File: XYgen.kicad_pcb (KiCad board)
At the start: 4 copper layers, 100 x 100 mm, 129 parts, among them J1 V_analog_in, J10 Mounting Hole, J11 Mounting Hole, J12 Mounting Hole, J13 Mounting Hole, J2 Ones, J3 Tens, J4 Hundreds, J5 Thousands, J6 Vin, J7 Blanking, J8 XOut, J9 YOut, Q1 MMBT3906, Q10 MMBT3906, Q11 MMBT3904, Q12 MMBT3906, Q13 MMBT3904, Q14 MMBFJ309, Q15 MMBT3904, Q2 MMBT3904, Q3 MMBT3906, Q4 MMBT3904, Q5 MMBT3906, Q6 MMBT3904, Q7 MMBFJ309, Q8 MMBT3906, Q9 MMBT3904, U1 40106, U10 LM358, U11 NE5532, U12 NE5532, U13 4052, U14 4052, U2 74HC123, U3 74HC08, U4 74HC32, U5 4040, U6 4511, U7 4051, U8 LM358, U9 LM358, Y1 32.768kHz

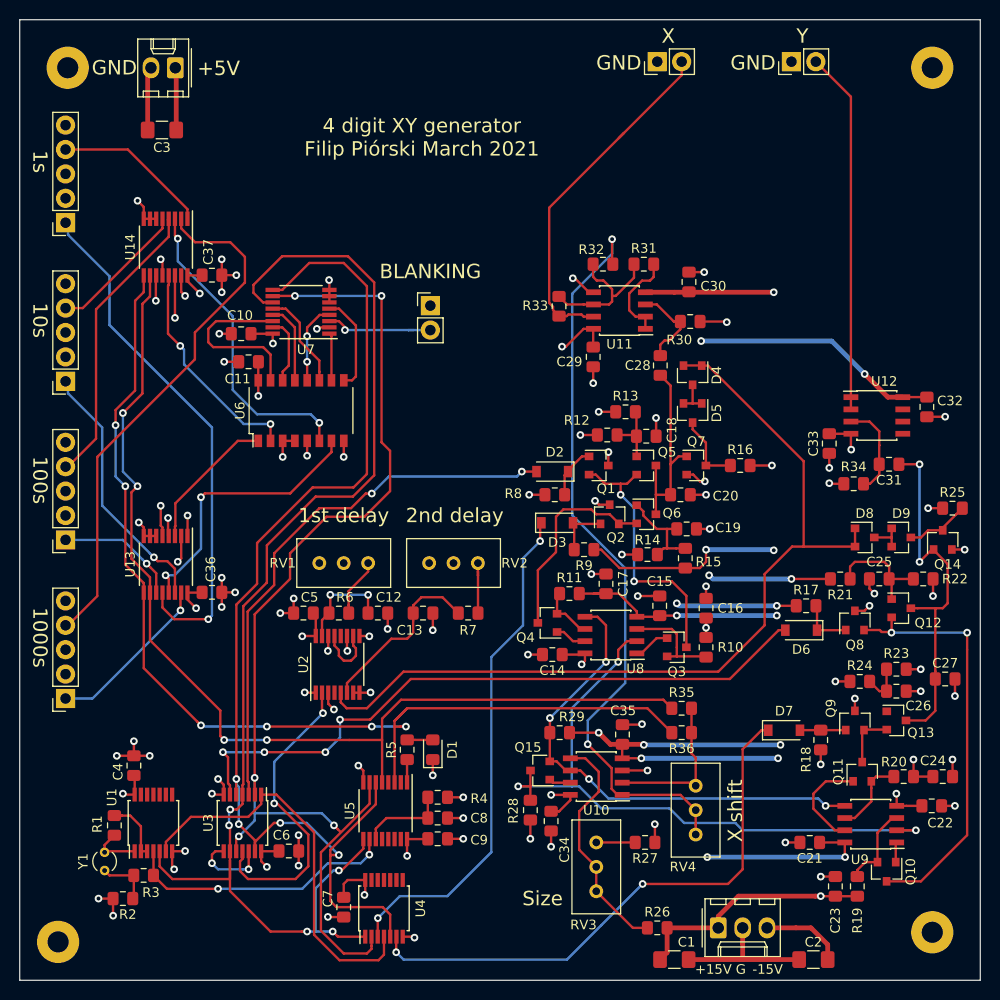
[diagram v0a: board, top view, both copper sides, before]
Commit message: Fixed some bugs, finished block symbols
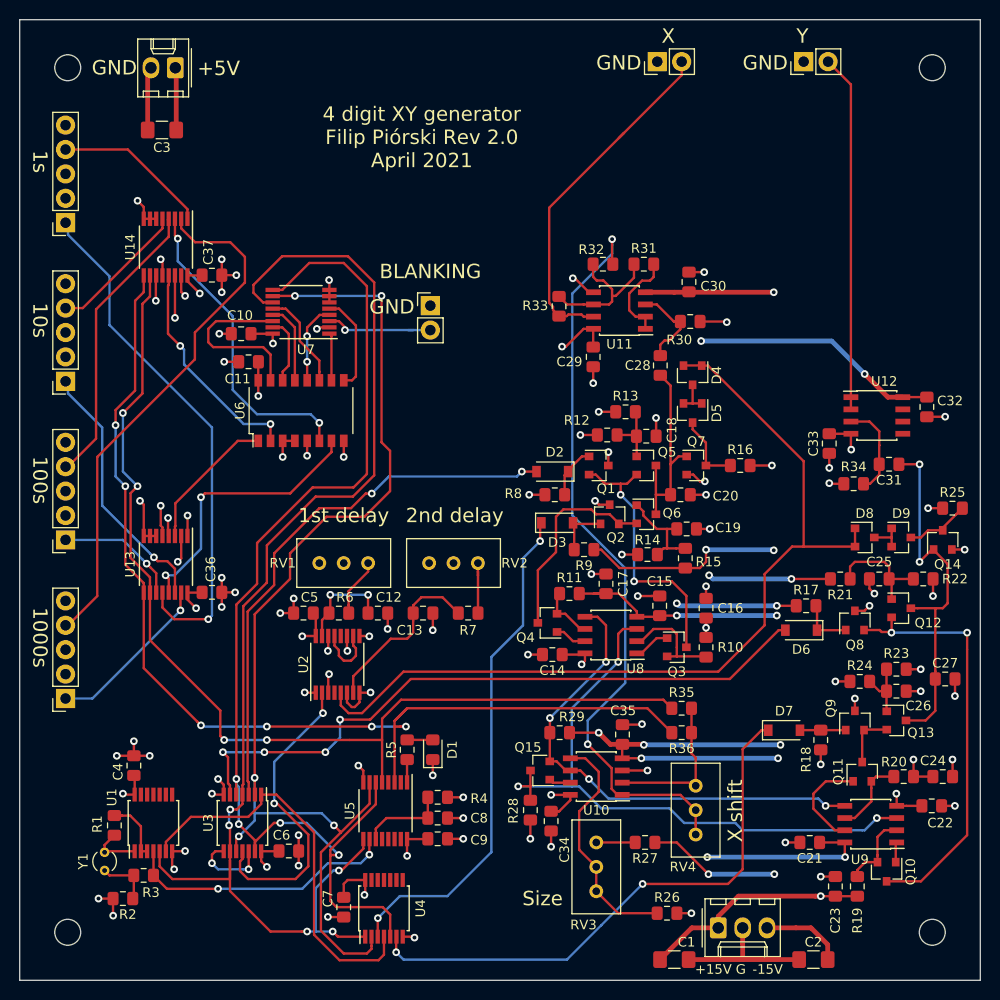
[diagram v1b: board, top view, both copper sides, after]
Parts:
- removed J10, J11, J12, J13: Mounting Hole, MountingHole:MountingHole_2.2mm_M2_Pad
- added H1: MountingHole, MountingHole:MountingHole_2.7mm_M2.5, F.Cu at (105.0, 40.0)
- added H2: MountingHole, MountingHole:MountingHole_2.7mm_M2.5, F.Cu at (105.0, 130.0)
- added H3: MountingHole, MountingHole:MountingHole_2.7mm_M2.5, F.Cu at (195.0, 130.0)
- added H4: MountingHole, MountingHole:MountingHole_2.7mm_M2.5, F.Cu at (195.0, 40.0)
- moved R26 1.83 mm to (167.4, 128.0)
- moved J9 1.27 mm to (181.6, 39.4)
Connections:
- R26 pad 2: +15V -> GND
- R27 pad 1: GND -> -15V
- U2 pad 6: Net-(C13-Pad1) -> GND
- U2 pad 7: GND -> Net-(C13-Pad1)
- U8 pad 2: /sheet601E8B82/HiCur -> Net-(Q3-Pad2)
- U8 pad 3: Net-(Q3-Pad2) -> /sheet601E8B82/HiCur
- U9 pad 2: /sheet601E8B82/HiCur -> Net-(Q10-Pad2)
- U9 pad 3: Net-(Q10-Pad2) -> /sheet601E8B82/HiCur
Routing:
- net -15V: track 126.4 -> 140.2 mm, vias 17 -> 19
- net GND: track 147.8 -> 152.7 mm
- net /sheet601E8B82/HiCur: track 68.2 -> 65.8 mm
- net Net-(C26-Pad1): track 4.47 -> 6.58 mm
- net +15V: track 117.6 -> 116.1 mm
- net Net-(Q10-Pad2): track 8.81 -> 8.03 mm
- net /sheet601E8B81/ZERO: track 92.3 -> 92.9 mm
- net /sheet601E8B86/YOut: track 37.7 -> 37.2 mm
- net Net-(Q3-Pad2): track 10.8 -> 11.4 mm
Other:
- board text added: "4 digit XY generator Filip Piórski Rev 2.0 April 2021"
- board text removed: "4 digit XY generator Filip Piórski March 2021"
